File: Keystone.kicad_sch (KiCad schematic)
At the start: 4 parts, among them SW1 SW_Push, SW2 SW_Push, SW3 SW_Push, U1 MOUDLE-SEEEDUINO-XIAO

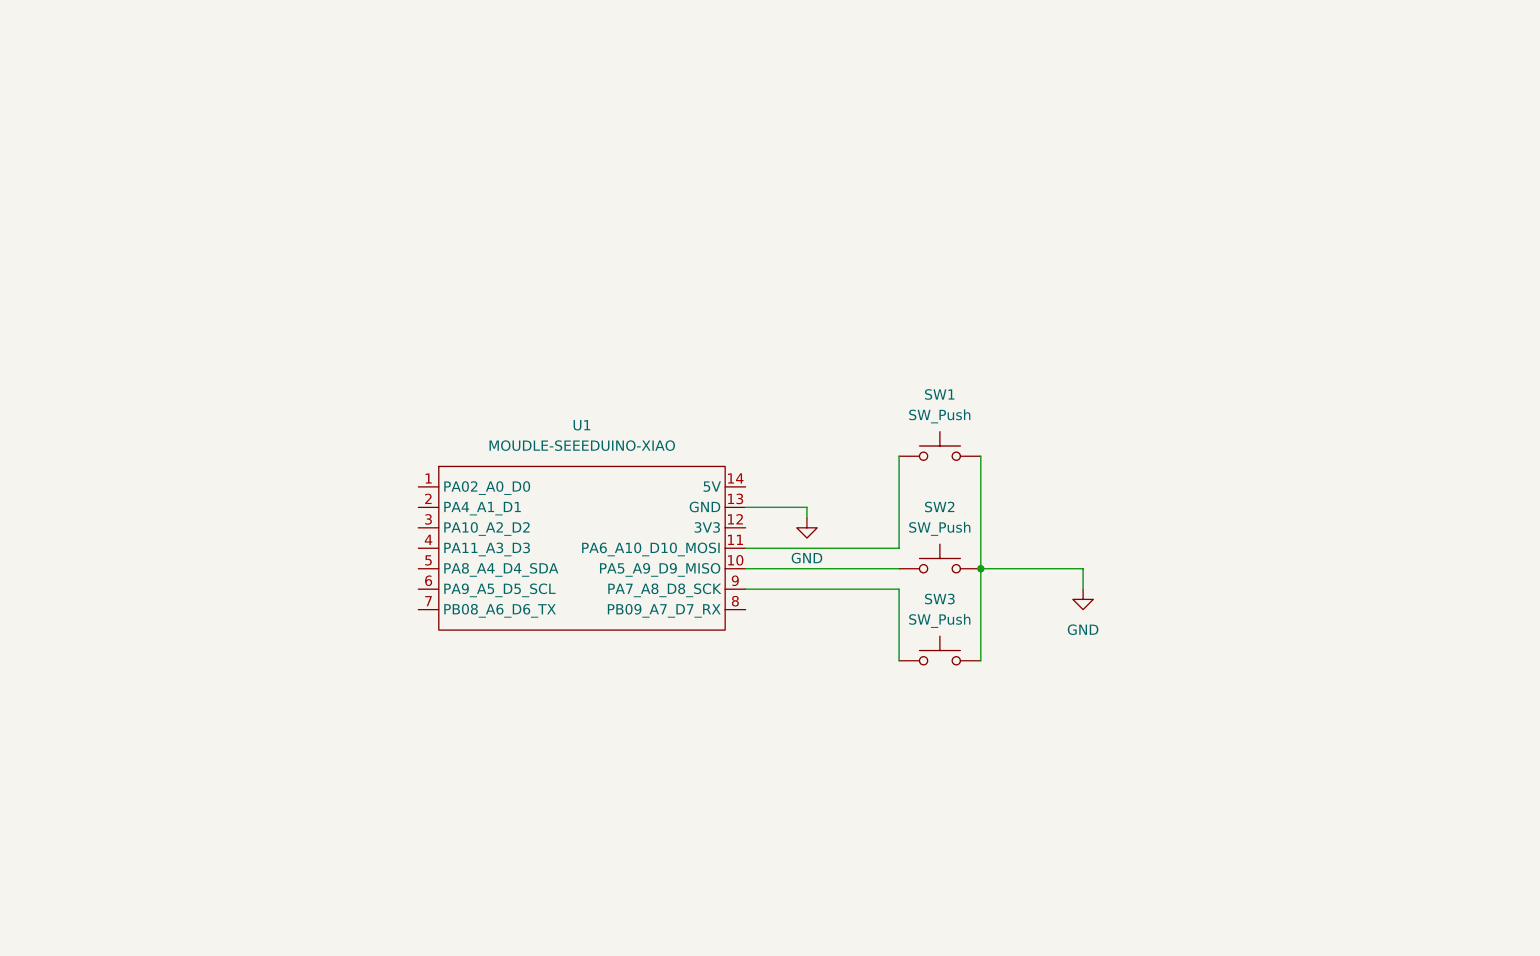
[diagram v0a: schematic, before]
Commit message: Assigned footprints for the schematics
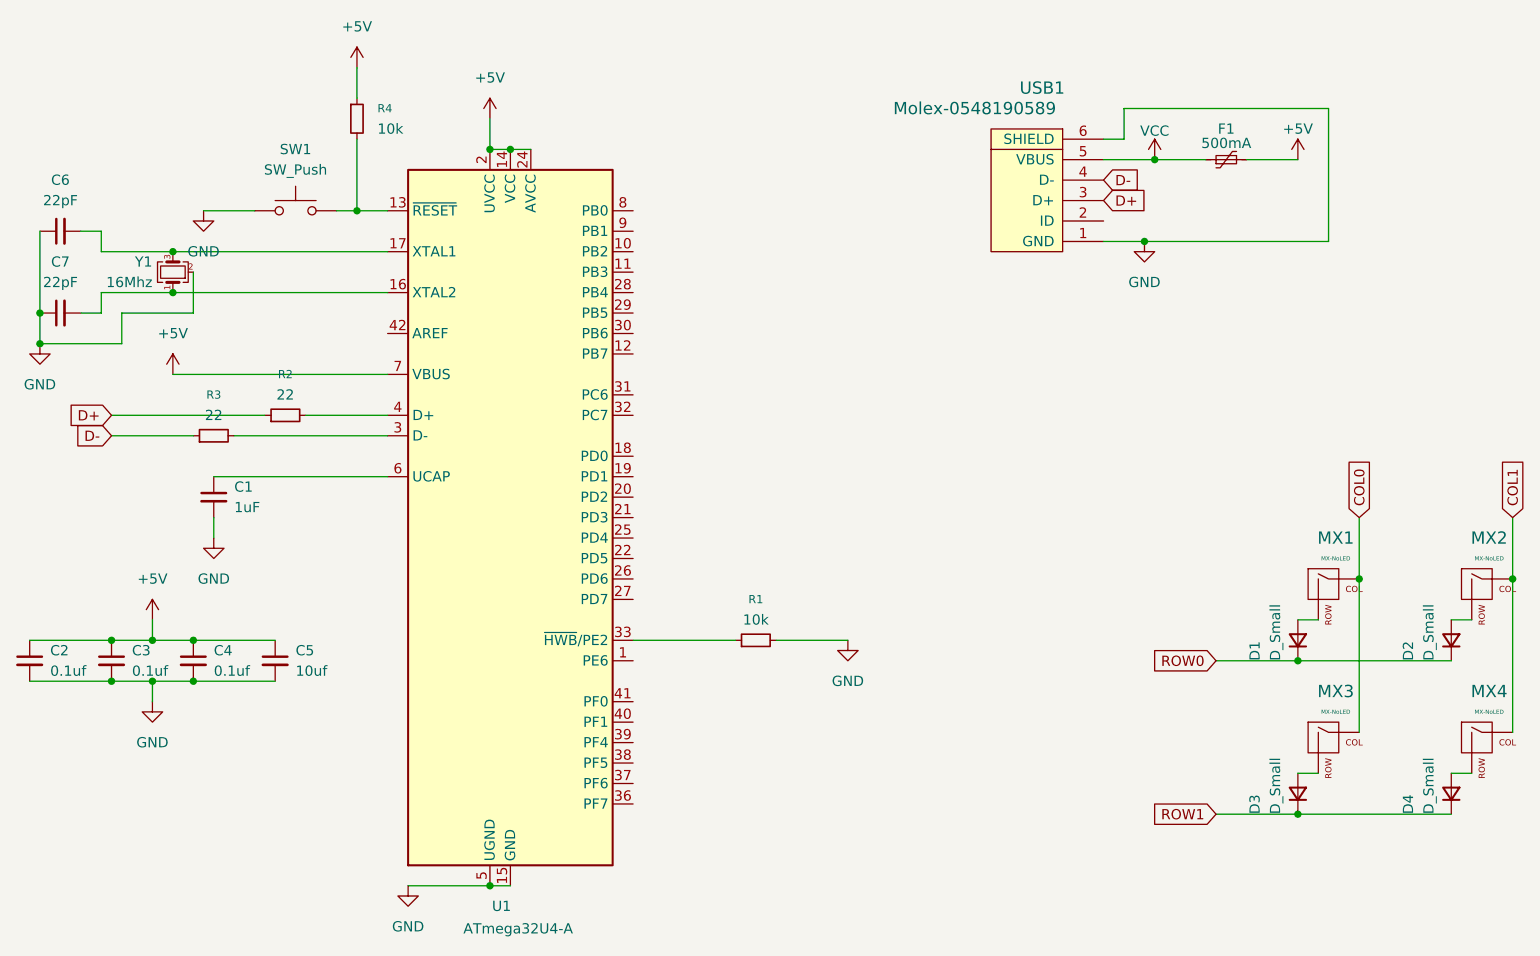
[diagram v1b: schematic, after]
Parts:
- removed SW2, SW3: SW_Push, Button_Switch_Keyboard:SW_Cherry_MX_1.00u_PCB, symbol Switch:SW_Push
- removed U1: MOUDLE-SEEEDUINO-XIAO, footprints:XIAO-Generic-Hybrid-14P-2.54-21X17.8MM, symbol XIAO_RP2040:MOUDLE-SEEEDUINO-XIAO
- added C1: 1uF, Capacitor_SMD:C_0805_2012Metric, symbol Device:C_Small
- added C2, C3, C4: 0.1uf, Capacitor_SMD:C_0805_2012Metric, symbol Device:C_Small
- added C5: 10uf, Capacitor_SMD:C_0805_2012Metric, symbol Device:C_Small
- added C6, C7: 22pF, Capacitor_SMD:C_0805_2012Metric, symbol Device:C_Small
- added D1, D2, D3, D4: D_Small, Diode_SMD:D_SOD-123, symbol Device:D_Small
- added F1: 500mA, Fuse:Fuse_1206_3216Metric, symbol Device:Polyfuse_Small
- added MX1, MX2, MX3, MX4: MX-NoLED, MX_Alps_Hybrid:MX-1U-NoLED, symbol MX_Alps_Hybrid:MX-NoLED
- added R1, R4: 10k, Resistor_SMD:R_0805_2012Metric, symbol Device:R_Small
- added R2, R3: 22, Resistor_SMD:R_0805_2012Metric, symbol Device:R_Small
- added U1: ATmega32U4-A, Package_QFP:TQFP-44_10x10mm_P0.8mm, symbol MCU_Microchip_ATmega:ATmega32U4-A
- added USB1: Molex-0548190589, random-keyboard-parts:Molex-0548190589, symbol random-keyboard-parts:Molex-0548190589
- added Y1: 16Mhz, Crystal:Crystal_SMD_3225-4Pin_3.2x2.5mm, symbol Device:Crystal_GND24_Small
- SW1: footprint Button_Switch_Keyboard:SW_Cherry_MX_1.00u_PCB -> random-keyboard-parts:SKQG-1155865
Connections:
- net GND: now also SW1.1, C1.2, C2.2, C3.2, C4.2, C5.2, C6.1, C7.1, R1.2, U1.15 (GND), U1.23 (GND), U1.35 (GND), U1.43 (GND), U1.5 (UGND), USB1.1 (GND), USB1.6 (SHIELD), Y1.2 (G), Y1.4 (G); no longer SW1.2
- new net: R3.2, U1.3 (D-)
- new net: D3.2 (A), MX3.2 (ROW)
- new net: R4.2, SW1.2, U1.13 (~{RESET})
- new net: D1.2 (A), MX1.2 (ROW)
- new net: D2.2 (A), MX2.2 (ROW)
- new net: C7.2, U1.16 (XTAL2), Y1.1
- new net: C1.1, U1.6 (UCAP)
- new net: C6.2, U1.17 (XTAL1), Y1.3
- new net: D4.2 (A), MX4.2 (ROW)
- new net: R2.2, U1.4 (D+)
- new net: R1.1, U1.33 (~{HWB}/PE2)
- new net +5V: C2.1, C3.1, C4.1, C5.1, F1.2, R4.1, U1.14 (VCC), U1.2 (UVCC), U1.24 (AVCC), U1.34 (VCC), U1.44 (AVCC), U1.7 (VBUS)
- new net COL0: MX1.1 (COL), MX3.1 (COL)
- new net COL1: MX2.1 (COL), MX4.1 (COL)
- new net D+: R2.1, USB1.3 (D+)
- new net D-: R3.1, USB1.4 (D-)
- new net ROW0: D1.1 (K), D2.1 (K)
- new net ROW1: D3.1 (K), D4.1 (K)
- new net VCC: F1.1, USB1.5 (VBUS)

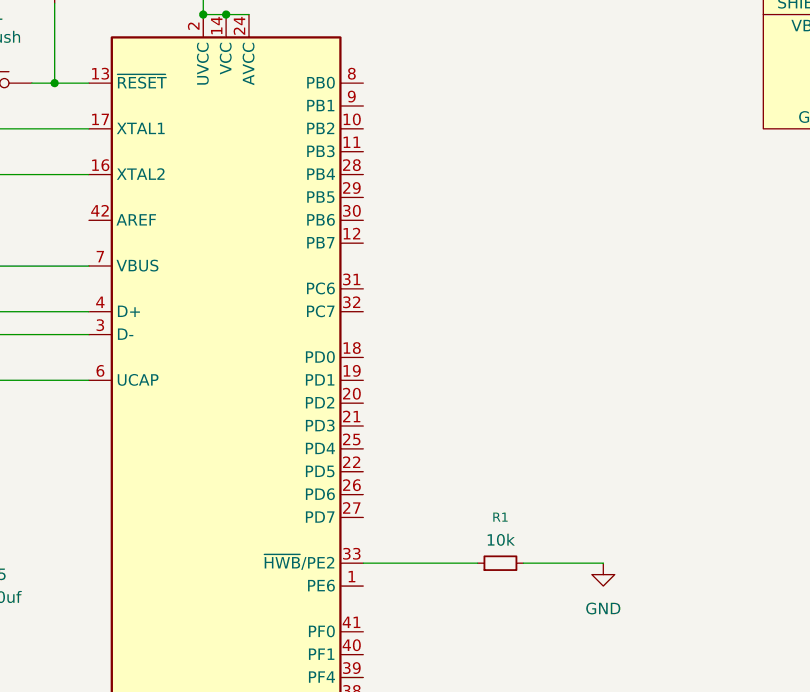
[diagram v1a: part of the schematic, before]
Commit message: Wired up components, realigned position
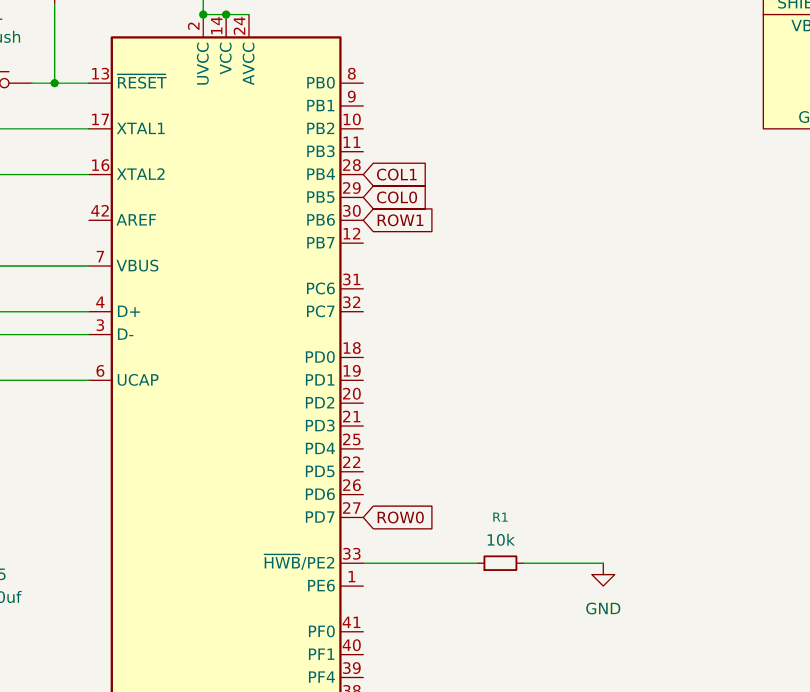
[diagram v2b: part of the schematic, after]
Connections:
- net COL0: now also U1.29 (PB5)
- net COL1: now also U1.28 (PB4)
- net ROW0: now also U1.27 (PD7)
- net ROW1: now also U1.30 (PB6)
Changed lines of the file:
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@@
+		)
+	)
+	(global_label "ROW1"
+		(shape input)
+		(at 95.25 60.96 0)
+		(fields_autoplaced yes)
+		(effects
+			(font
+				(size 1.27 1.27)
+			)
+			(justify left)
+		)
+		(property "Intersheetrefs" "${INTERSHEET_REFS}"
+			(at 103.4966 60.96 0)
+			(hide yes)
+			(show_name no)
+			(do_not_autoplace no)
+			(effects
+				(font
+					(size 1.27 1.27)
+				)
+				(justify left)
+			)
 		)
 	)
@@
 		)
 	)
+	(global_label "COL1"
+		(shape input)
+		(at 95.25 55.88 0)
+		(fields_autoplaced yes)
+		(effects
+			(font
+				(size 1.27 1.27)
+			)
+			(justify left)
+		)
+		(property "Intersheetrefs" "${INTERSHEET_REFS}"
+			(at 103.0733 55.88 0)
+			(hide yes)
+			(show_name no)
+			(do_not_autoplace no)
+			(effects
+				(font
+					(size 1.27 1.27)
+				)
+				(justify left)
+			)
+		)
+	)
 	(global_label "D+"
 		(shape input)
@@
 			)
 		)
+	)
+	(global_label "COL0"
+		(shape input)
+		(at 95.25 58.42 0)
+		(fields_autoplaced yes)
+		(effects
+			(font
+				(size 1.27 1.27)
+			)
+			(justify left)
+		)
+		(property "Intersheetrefs" "${INTERSHEET_REFS}"
+			(at 103.0733 58.42 0)
+			(hide yes)
+			(show_name no)
+			(do_not_autoplace no)
+			(effects
+				(font
+					(size 1.27 1.27)
+				)
+				(justify left)
+			)
+		)
+	)
+	(global_label "ROW0"
+		(shape input)
+		(at 95.25 93.98 0)
+		(fields_autoplaced yes)
+		(effects
+			(font
+				(size 1.27 1.27)
+			)
+			(justify left)
+		)
+		(property "Intersheetrefs" "${INTERSHEET_REFS}"
+			(at 103.4966 93.98 0)
+			(hide yes)
+			(show_name no)
+			(do_not_autoplace no)
+			(effects
+				(font
+					(size 1.27 1.27)
+				)
+				(justify left)
+			)
+		)
